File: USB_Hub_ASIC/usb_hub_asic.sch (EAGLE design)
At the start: 105 parts, among them J1 CONN_RCPT_USB3.0_TYPEB_9POS_R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, J2 CONN_RCPT_USB3.0_TYPEA_9POS_R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, J3 CONN_RCPT_USB3.0_TYPEA_9POS_R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, J4 CONN_RCPT_USB3.0_TYPEA_9POS_R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, J5 CONN_RCPT_USB3.0_TYPEA_9POS_R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, Q1 26M, U1 IC_MCP1603LT-330_3.3V_500MA_B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, U2 IC_CYUSB3314_QUAD_USB3.0_HUB, U3 IC_LM3674MF-1.2/NOPB_1.2V_600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

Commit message: Board layout, need to place config resistors
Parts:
- removed S1: MOMENTARY-SWITCH-SPST-SMD-12MM, SparkFun-Switches:MOMENTARY-SWITCH-SPST-SMD-12MM
- added SW1: RESET, USB_Hub_ASIC:SW_SPDT_TLSMDT3C020GLFS
- C15, C17: device rcl:C-USC0805 -> rcl:C-USC0603
- renumbered J1 to US, J2 to DS1, J3 to DS3, J4 to DS2, J5 to DS4
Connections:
- net GND: now also SW1.A; no longer S1.2
- net RESETIN: now also SW1.D; no longer S1.1

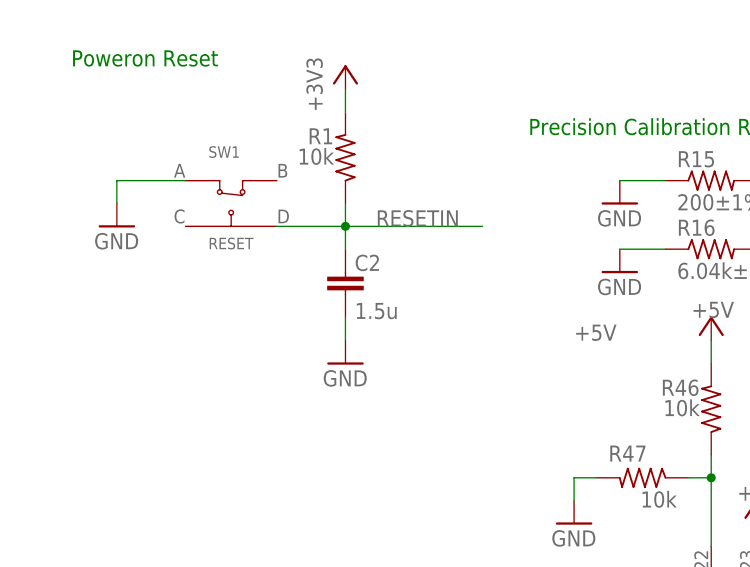
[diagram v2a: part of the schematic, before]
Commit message: start over on board design w/ 4 layers
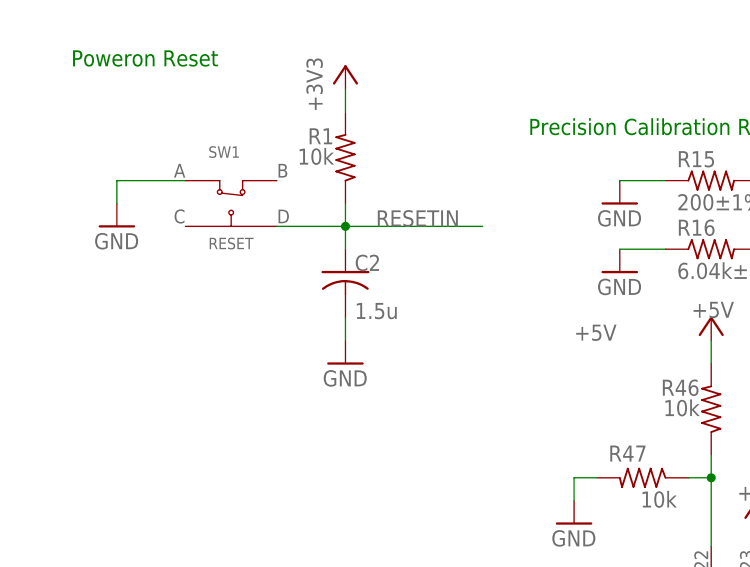
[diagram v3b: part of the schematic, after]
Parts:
- C2: device SparkFun-Capacitors:CAP-0603 -> rcl:C-USC0603
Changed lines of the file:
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@@
 <drawing>
 <settings>
-<setting alwaysvectorfont="no"/>
+<setting alwaysvectorfont="yes"/>
 <setting verticaltext="up"/>
 </settings>
@@
 <part name="C11" library="rcl" library_urn="urn:adsk.eagle:library:334" deviceset="C-US" device="C0603" package3d_urn="urn:adsk.eagle:package:23616/2" value="22u"/>
 <part name="C10" library="rcl" library_urn="urn:adsk.eagle:library:334" deviceset="C-US" device="C0603" package3d_urn="urn:adsk.eagle:package:23616/2" value="22u"/>
-<part name="C2" library="SparkFun-Capacitors" deviceset="CAP" device="-0603" value="1.5u"/>
+<part name="C2" library="rcl" library_urn="urn:adsk.eagle:library:334" deviceset="C-US" device="C0603" package3d_urn="urn:adsk.eagle:package:23616/2" value="1.5u"/>
 <part name="R1" library="rcl" library_urn="urn:adsk.eagle:library:334" deviceset="R-US_" device="R0603" package3d_urn="urn:adsk.eagle:package:23555/3" value="10k"/>
 <part name="R29" library="rcl" library_urn="urn:adsk.eagle:library:334" deviceset="R-US_" device="R0603" package3d_urn="urn:adsk.eagle:package:23555/3" value="10k"/>
@@
 <attribute name="VALUE" x="130.556" y="130.429" size="1.778" layer="96"/>
 </instance>
-<instance part="C2" gate="G$1" x="38.1" y="144.78" smashed="yes" rot="MR0">
+<instance part="C2" gate="G$1" x="38.1" y="147.32" smashed="yes" rot="MR0">
 <attribute name="NAME" x="39.116" y="149.225" size="1.778" layer="95" rot="MR180"/>
 <attribute name="VALUE" x="39.116" y="143.891" size="1.778" layer="96" rot="MR180"/>
@@
 <segment>
 <pinref part="C2" gate="G$1" pin="2"/>
+<pinref part="GND2" gate="1" pin="GND"/>
 <wire x1="38.1" y1="142.24" x2="38.1" y2="139.7" width="0.1524" layer="91"/>
-<pinref part="GND2" gate="1" pin="GND"/>
-</segment>
-<segment>
+</segment>
+<segment>
